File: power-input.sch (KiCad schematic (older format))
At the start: 13 parts, among them Q1 WST03P06

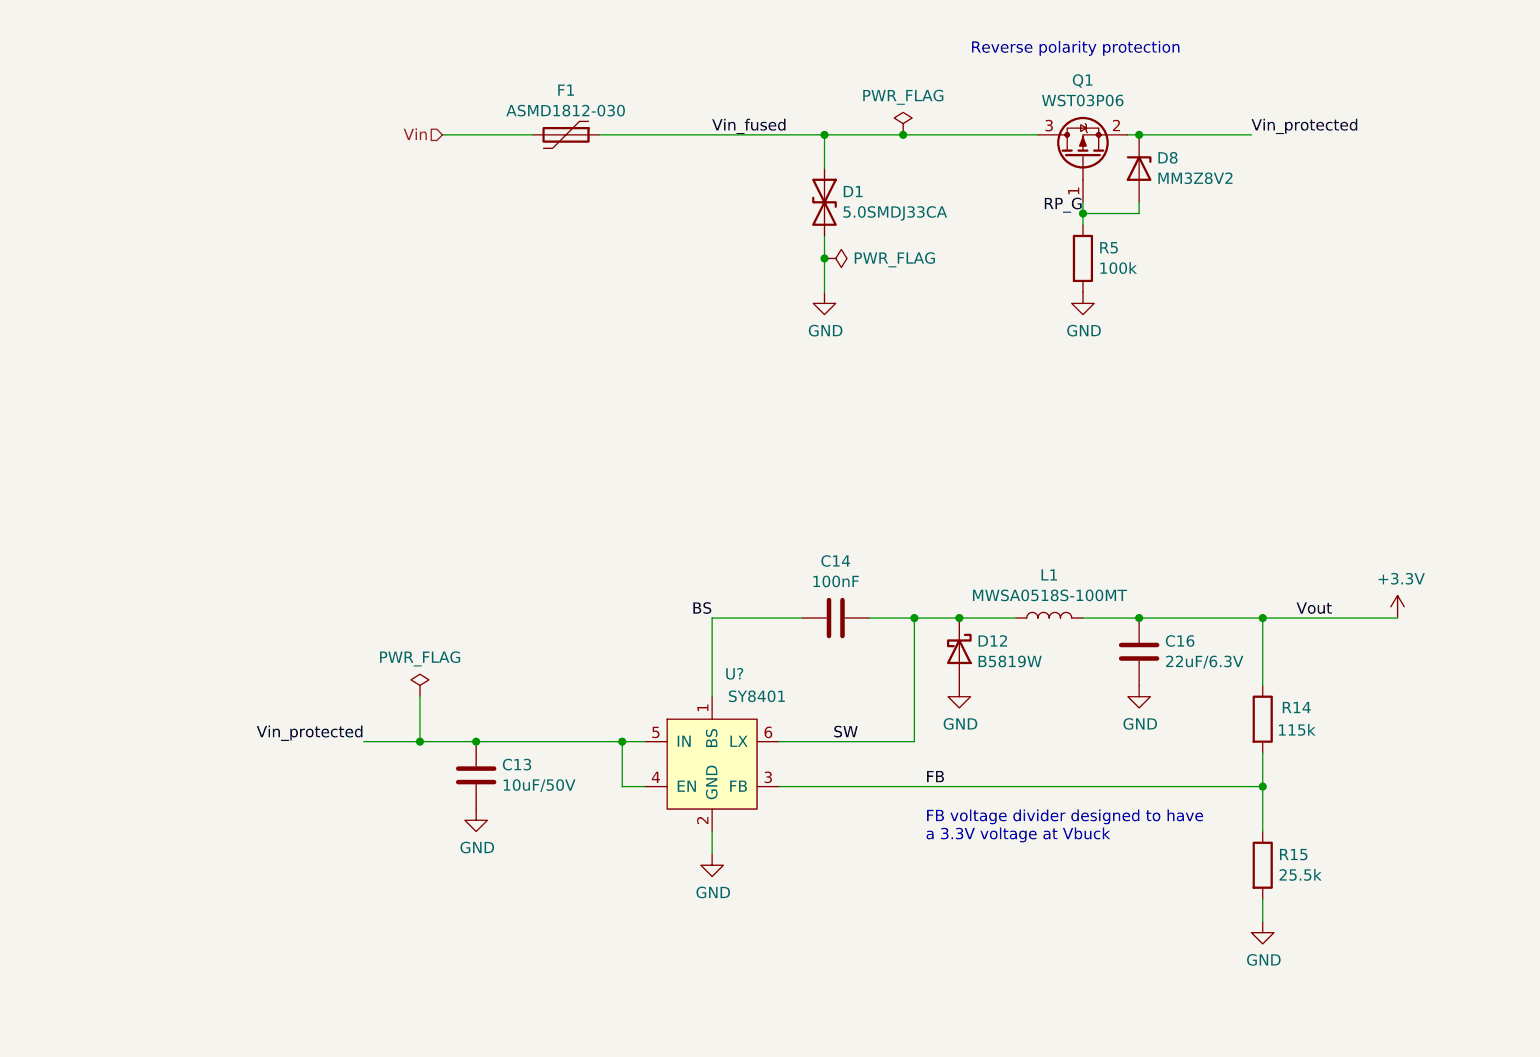
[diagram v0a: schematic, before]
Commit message: Update according to comments
Also add missing connectors and update the fuses
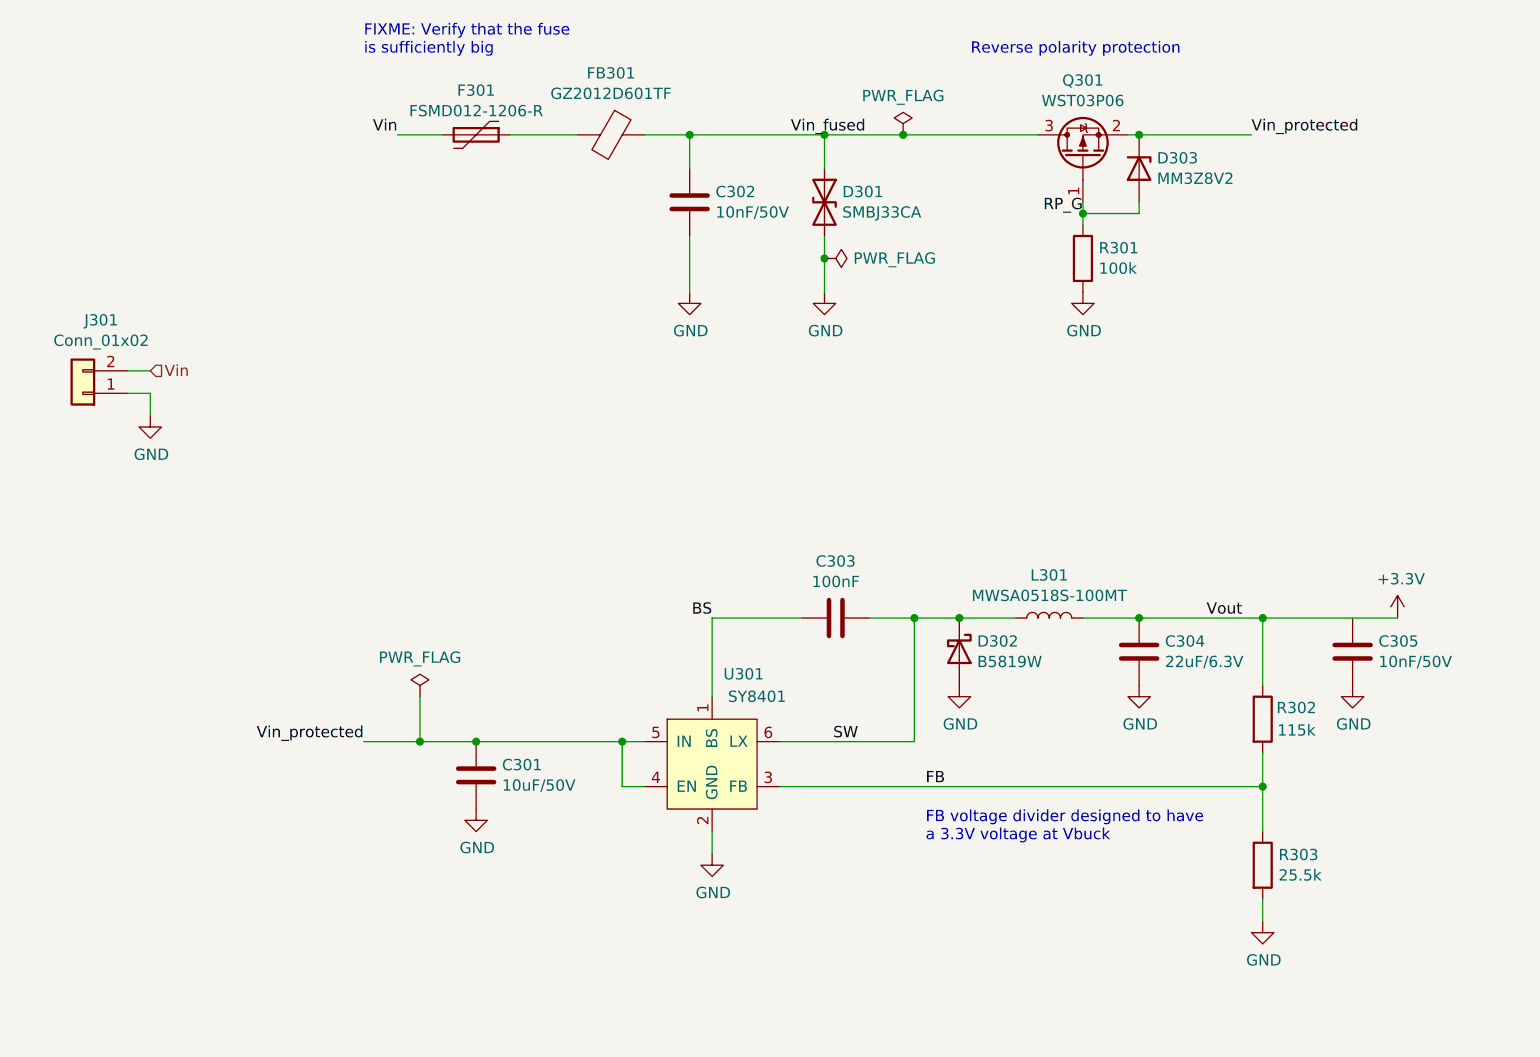
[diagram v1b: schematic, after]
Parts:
- removed D1: 5.0SMDJ33CA, Diode_SMD:D_SMC, symbol Device:D_TVS
- removed U?: SY8401, symbol SH-ESP32:SY8401
- added C302, C305: 10nF/50V, symbol Device:C
- added D301: SMBJ33CA, Diode_SMD:D_SMB, symbol Device:D_TVS
- added FB301: GZ2012D601TF, symbol Device:Ferrite_Bead
- added J301: Conn_01x02, symbol Connector_Generic:Conn_01x02
- added U301: SY8401, symbol SH-ESP32:SY8401
- F301: renamed from F1; value ASMD1812-030 -> FSMD012-1206-R
- renumbered C13 to C301, C14 to C303, C16 to C304, D12 to D302, D8 to D303, L1 to L301, Q1 to Q301, R5 to R301, R14 to R302, R15 to R303
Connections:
- net BS: now also U301.1 (BS)
- net FB: now also U301.3 (FB)
- net GND: now also C302.2, C305.2, D301.2 (A2), J301.1 (Pin_1), U301.2 (GND)
- net SW: now also U301.6 (LX)
- net Vin: now also J301.2 (Pin_2)
- net Vin_fused: now also C302.1, D301.1 (A1), FB301.1; no longer F301.1
- net Vin_protected: now also U301.4 (EN), U301.5 (IN)
- new net: F301.1, FB301.2
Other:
- note added: "FIXME: Verify that the fuse\nis sufficiently big"
- moved on the sheet: F301

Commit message: Rough PCB layout
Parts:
- C302, C305: footprint (none) -> Capacitor_SMD:C_0402_1005Metric
- D302: footprint (none) -> Diode_SMD:D_SOD-123
- F301: footprint (none) -> Fuse:Fuse_1206_3216Metric
- FB301: footprint (none) -> Inductor_SMD:L_0805_2012Metric
- J301: footprint (none) -> Connector_Phoenix_MC:PhoenixContact_MCV_1,5_2-G-3.81_1x02_P3.81mm_Vertical
- L301: footprint (none) -> Inductor_SMD:L_Sunlord_MWSA0518_5.4x5.2mm
- R301: footprint Resistor_SMD:R_0603_1608Metric -> Resistor_SMD:R_0402_1005Metric
- U301: footprint (none) -> Package_TO_SOT_SMD:SOT-23-6
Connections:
- net +3V3: now also C305.1
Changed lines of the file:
@@
 F 0 "F301" V 3653 2100 50  0000 C CNN
 F 1 "FSMD012-1206-R" V 3744 2100 50  0000 C CNN
-F 2 "" V 3780 2100 50  0001 C CNN
+F 2 "Fuse:Fuse_1206_3216Metric" V 3780 2100 50  0001 C CNN
 F 3 "~" H 3850 2100 50  0001 C CNN
 F 4 "" H 3850 2100 50  0001 C CNN "LCSC"
@@
 	1    0    0    -1
 $EndComp
-Wire Wire Line
-	5400 2550 5400 2650
-Connection ~ 5400 2650
-Wire Wire Line
-	5400 2650 5400 2800
 $Comp
 L Transistor_FET:Si2371EDS Q?
@@
 F 0 "R301" H 6620 2696 50  0000 L CNN
 F 1 "100k" H 6620 2605 50  0000 L CNN
-F 2 "Resistor_SMD:R_0603_1608Metric" V 6480 2650 50  0001 C CNN
+F 2 "Resistor_SMD:R_0402_1005Metric" V 6480 2650 50  0001 C CNN
 F 3 "~" H 6550 2650 50  0001 C CNN
 F 4 "C25803" H 6550 2650 50  0001 C CNN "LCSC"
@@
 Wire Wire Line
 	5750 2100 6350 2100
-$Comp
-L power:PWR_FLAG #FLG?
-U 1 1 5E475BD3
-P 5400 2650
-AR Path="/5E475BD3" Ref="#FLG?"  Part="1"
-AR Path="/5E460E30/5E475BD3" Ref="#FLG?"  Part="1"
-AR Path="/5F6FAF6E/5E475BD3" Ref="#FLG0302"  Part="1"
-F 0 "#FLG0302" H 5400 2725 50  0001 C CNN
-F 1 "PWR_FLAG" V 5400 2778 50  0000 L CNN
-F 2 "" H 5400 2650 50  0001 C CNN
-F 3 "~" H 5400 2650 50  0001 C CNN
-	1    5400 2650
-	0    1    -1   0
-$EndComp
 Text Label 6550 2450 2    50   ~ 0
 RP_G
@@
 F 0 "L301" V 6590 4250 50  0000 C CNN
 F 1 "MWSA0518S-100MT" V 6499 4250 50  0000 C CNN
-F 2 "" H 6400 4250 50  0001 C CNN
+F 2 "Inductor_SMD:L_Sunlord_MWSA0518_5.4x5.2mm" H 6400 4250 50  0001 C CNN
 F 3 "~" H 6400 4250 50  0001 C CNN
 F 4 "" V 6400 4250 50  0001 C CNN "URL"
@@
 F 0 "D302" V 5954 4479 50  0000 L CNN
 F 1 "B5819W" V 6045 4479 50  0000 L CNN
-F 2 "" H 6000 4400 50  0001 C CNN
+F 2 "Diode_SMD:D_SOD-123" H 6000 4400 50  0001 C CNN
 F 3 "~" H 6000 4400 50  0001 C CNN
 F 4 "" V 6000 4400 50  0001 C CNN "Notes"
@@
 F 0 "FB301" V 4176 2100 50  0000 C CNN
 F 1 "GZ2012D601TF" V 4267 2100 50  0000 C CNN
-F 2 "" V 4380 2100 50  0001 C CNN
+F 2 "Inductor_SMD:L_0805_2012Metric" V 4380 2100 50  0001 C CNN
 F 3 "~" H 4450 2100 50  0001 C CNN
 	1    4450 2100
@@
 F 0 "C302" H 4915 2446 50  0000 L CNN
 F 1 "10nF/50V" H 4915 2355 50  0000 L CNN
-F 2 "" H 4838 2250 50  0001 C CNN
+F 2 "Capacitor_SMD:C_0402_1005Metric" H 4838 2250 50  0001 C CNN
 F 3 "~" H 4800 2400 50  0001 C CNN
 	1    4800 2400
@@
 F 0 "U301" H 4950 5400 50  0000 L CNN
 F 1 "SY8401" H 5100 5300 50  0000 C CNN
-F 2 "" H 4750 4950 50  0001 C CNN
+F 2 "Package_TO_SOT_SMD:SOT-23-6" H 4750 4950 50  0001 C CNN
 F 3 "" H 4750 4950 50  0001 C CNN
 	1    4900 4950
@@
 	6800 4250 7350 4250
 Wire Wire Line
-	7350 4250 7950 4250
+	7350 4250 7750 4250
 Connection ~ 7350 4250
 Connection ~ 7350 5000
@@
 F 0 "C305" H 7865 4446 50  0000 L CNN
 F 1 "10nF/50V" H 7865 4355 50  0000 L CNN
-F 2 "" H 7788 4250 50  0001 C CNN
+F 2 "Capacitor_SMD:C_0402_1005Metric" H 7788 4250 50  0001 C CNN
 F 3 "~" H 7750 4400 50  0001 C CNN
 	1    7750 4400
@@
 F 0 "J301" H 2018 2925 50  0000 C CNN
 F 1 "Conn_01x02" H 2018 3016 50  0000 C CNN
-F 2 "" H 2100 3250 50  0001 C CNN
+F 2 "Connector_Phoenix_MC:PhoenixContact_MCV_1,5_2-G-3.81_1x02_P3.81mm_Vertical" H 2100 3250 50  0001 C CNN
 F 3 "~" H 2100 3250 50  0001 C CNN
 	1    2100 3250
@@
 Wire Wire Line
 	2400 3150 2300 3150
-Text HLabel 2400 3150 2    50   Input ~ 0
-Vin
 $Comp
 L Device:D_TVS D?
@@
 Text Notes 3350 1750 0    50   ~ 0
 FIXME: Verify that the fuse\nis sufficiently big
+Text Label 2400 3150 0    50   ~ 0
+Vin
+Wire Wire Line
+	5400 2550 5400 2800
+Connection ~ 7750 4250
+Wire Wire Line
+	7750 4250 7950 4250
 $EndSCHEMATC

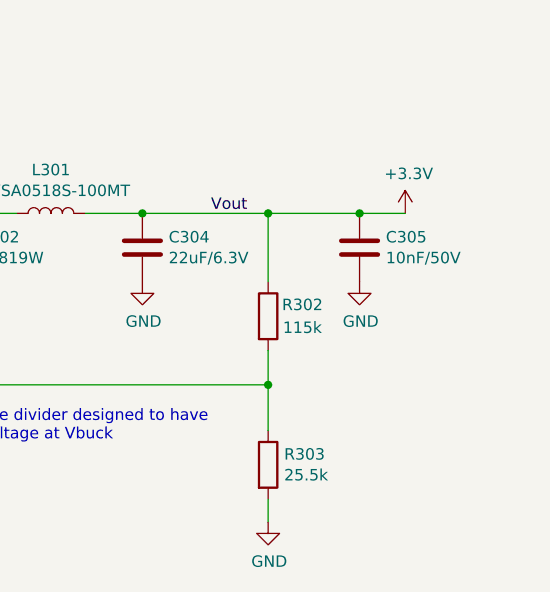
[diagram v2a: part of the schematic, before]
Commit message: Specified JLCPCB footprints for components
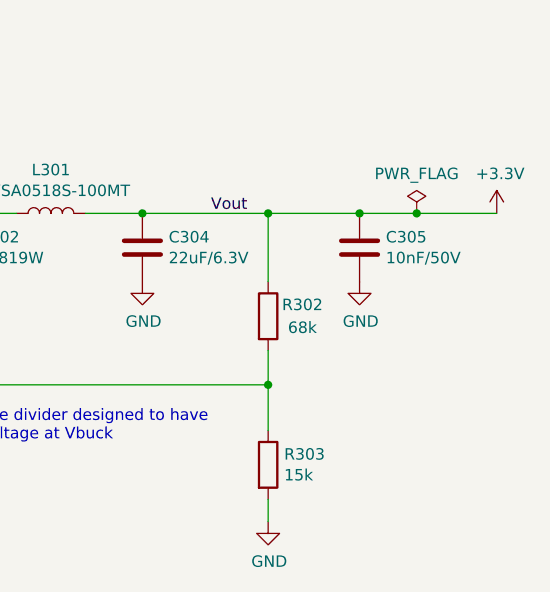
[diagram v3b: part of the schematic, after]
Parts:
- C302, C305: LCSC (none) -> C15195
- C303: footprint Capacitor_SMD:C_0603_1608Metric -> Capacitor_SMD:C_0402_1005Metric; LCSC C14663 -> C1525
- F301: LCSC (none) -> C220144
- FB301: LCSC (none) -> C1017
- J301: LCSC (none) -> C8396
- R301: LCSC C25803 -> C25741
- R302: value 115k -> 68k; LCSC C25747 -> C36871
- R303: value 25.5k -> 15k; LCSC C26970 -> C25756
- U301: LCSC (none) -> C125906
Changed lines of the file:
@@
 F 2 "Fuse:Fuse_1206_3216Metric" V 3780 2100 50  0001 C CNN
 F 3 "~" H 3850 2100 50  0001 C CNN
-F 4 "" H 3850 2100 50  0001 C CNN "LCSC"
+F 4 "C220144" H 3850 2100 50  0001 C CNN "LCSC"
 	1    3850 2100
 	0    1    1    0
@@
 F 2 "Resistor_SMD:R_0402_1005Metric" V 6480 2650 50  0001 C CNN
 F 3 "~" H 6550 2650 50  0001 C CNN
-F 4 "C25803" H 6550 2650 50  0001 C CNN "LCSC"
+F 4 "C25741" H 6550 2650 50  0001 C CNN "LCSC"
 	1    6550 2650
 	1    0    0    -1
@@
 F 0 "C303" V 5198 4250 50  0000 C CNN
 F 1 "100nF" V 5289 4250 50  0000 C CNN
-F 2 "Capacitor_SMD:C_0603_1608Metric" H 5488 4100 50  0001 C CNN
+F 2 "Capacitor_SMD:C_0402_1005Metric" H 5488 4100 50  0001 C CNN
 F 3 "~" H 5450 4250 50  0001 C CNN
-F 4 "C14663" H 5450 4250 50  0001 C CNN "LCSC"
+F 4 "C1525" H 5450 4250 50  0001 C CNN "LCSC"
 	1    5450 4250
 	0    1    1    0
@@
 L power:+3.3V #PWR0310
 U 1 1 5F80ACBB
-P 7950 4250
-F 0 "#PWR0310" H 7950 4100 50  0001 C CNN
-F 1 "+3.3V" H 7965 4423 50  0000 C CNN
-F 2 "" H 7950 4250 50  0001 C CNN
-F 3 "" H 7950 4250 50  0001 C CNN
-	1    7950 4250
+P 8350 4250
+F 0 "#PWR0310" H 8350 4100 50  0001 C CNN
+F 1 "+3.3V" H 8365 4423 50  0000 C CNN
+F 2 "" H 8350 4250 50  0001 C CNN
+F 3 "" H 8350 4250 50  0001 C CNN
+	1    8350 4250
 	1    0    0    -1
 $EndComp
@@
 F 2 "Inductor_SMD:L_0805_2012Metric" V 4380 2100 50  0001 C CNN
 F 3 "~" H 4450 2100 50  0001 C CNN
+F 4 "C1017" H 4450 2100 50  0001 C CNN "LCSC"
 	1    4450 2100
 	0    1    1    0
@@
 F 2 "Capacitor_SMD:C_0402_1005Metric" H 4838 2250 50  0001 C CNN
 F 3 "~" H 4800 2400 50  0001 C CNN
+F 4 "C15195" H 4800 2400 50  0001 C CNN "LCSC"
 	1    4800 2400
 	1    0    0    -1
@@
 F 2 "Package_TO_SOT_SMD:SOT-23-6" H 4750 4950 50  0001 C CNN
 F 3 "" H 4750 4950 50  0001 C CNN
+F 4 "C125906" H 4900 4950 50  0001 C CNN "LCSC"
 	1    4900 4950
 	1    0    0    -1
@@
 AR Path="/5F6FAF6E/5CA62D90" Ref="R302"  Part="1"
 F 0 "R302" H 7500 4750 50  0000 C CNN
-F 1 "115k" H 7500 4650 50  0000 C CNN
+F 1 "68k" H 7500 4650 50  0000 C CNN
 F 2 "Resistor_SMD:R_0402_1005Metric" V 7280 4700 50  0001 C CNN
 F 3 "~" H 7350 4700 50  0001 C CNN
-F 4 "C25747" H 7350 4700 50  0001 C CNN "LCSC"
+F 4 "C36871" H 7350 4700 50  0001 C CNN "LCSC"
 	1    7350 4700
 	1    0    0    -1
@@
 AR Path="/5F6FAF6E/5CA62D89" Ref="R303"  Part="1"
 F 0 "R303" H 7420 5396 50  0000 L CNN
-F 1 "25.5k" H 7420 5305 50  0000 L CNN
+F 1 "15k" H 7420 5305 50  0000 L CNN
 F 2 "Resistor_SMD:R_0402_1005Metric" V 7280 5350 50  0001 C CNN
 F 3 "~" H 7350 5350 50  0001 C CNN
-F 4 "C26970" H 7350 5350 50  0001 C CNN "LCSC"
+F 4 "C25756" H 7350 5350 50  0001 C CNN "LCSC"
 	1    7350 5350
 	1    0    0    -1
@@
 F 2 "Capacitor_SMD:C_0402_1005Metric" H 7788 4250 50  0001 C CNN
 F 3 "~" H 7750 4400 50  0001 C CNN
+F 4 "C15195" H 7750 4400 50  0001 C CNN "LCSC"
 	1    7750 4400
 	1    0    0    -1
@@
 F 2 "Connector_Phoenix_MC:PhoenixContact_MCV_1,5_2-G-3.81_1x02_P3.81mm_Vertical" H 2100 3250 50  0001 C CNN
 F 3 "~" H 2100 3250 50  0001 C CNN
+F 4 "C8396" H 2100 3250 50  0001 C CNN "LCSC"
 	1    2100 3250
 	-1   0    0    1
@@
 Connection ~ 7750 4250
 Wire Wire Line
-	7750 4250 7950 4250
+	7750 4250 8000 4250
+$Comp
+L power:PWR_FLAG #FLG0101
+U 1 1 5FAE11E1
+P 8000 4250
+F 0 "#FLG0101" H 8000 4325 50  0001 C CNN
+F 1 "PWR_FLAG" H 8000 4423 50  0000 C CNN
+F 2 "" H 8000 4250 50  0001 C CNN
+F 3 "~" H 8000 4250 50  0001 C CNN
+	1    8000 4250
+	1    0    0    -1
+$EndComp
+Connection ~ 8000 4250
+Wire Wire Line
+	8000 4250 8350 4250
 $EndSCHEMATC

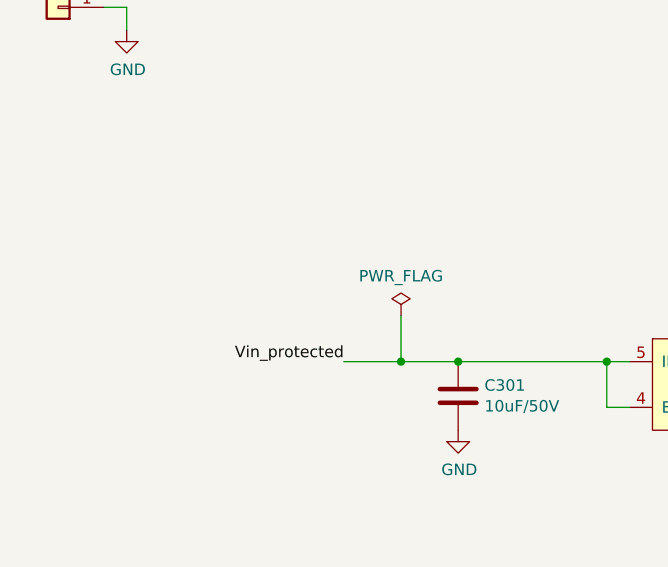
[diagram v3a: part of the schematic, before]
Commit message: Trace USB 5V to buck converter input
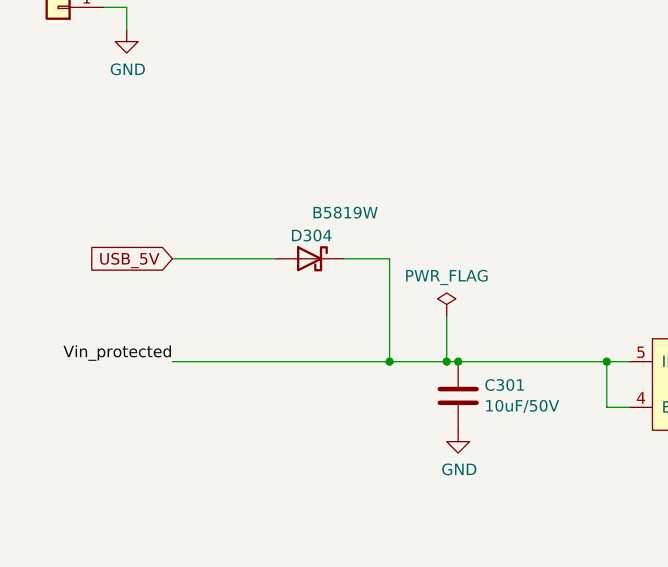
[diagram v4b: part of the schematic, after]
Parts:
- added D304: B5819W, Diode_SMD:D_SOD-123, symbol Device:D_Schottky
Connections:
- net Vin_protected: now also D304.1 (K)
- new net USB_5V: D304.2 (A)
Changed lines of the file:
@@
 L power:PWR_FLAG #FLG?
 U 1 1 5CA62DDA
-P 3600 4600
+P 3800 4600
 AR Path="/5C3476D8/5CA62DDA" Ref="#FLG?"  Part="1"
 AR Path="/5CA65CC5/5CA62DDA" Ref="#FLG?"  Part="1"
 AR Path="/5F6FAF6E/5CA62DDA" Ref="#FLG0301"  Part="1"
-F 0 "#FLG0301" H 3600 4675 50  0001 C CNN
-F 1 "PWR_FLAG" H 3600 4774 50  0000 C CNN
-F 2 "" H 3600 4600 50  0001 C CNN
-F 3 "~" H 3600 4600 50  0001 C CNN
-	1    3600 4600
-	1    0    0    -1
-$EndComp
-Wire Wire Line
-	3600 4600 3600 4800
-Connection ~ 3600 4800
+F 0 "#FLG0301" H 3800 4675 50  0001 C CNN
+F 1 "PWR_FLAG" H 3800 4774 50  0000 C CNN
+F 2 "" H 3800 4600 50  0001 C CNN
+F 3 "~" H 3800 4600 50  0001 C CNN
+	1    3800 4600
+	1    0    0    -1
+$EndComp
+Wire Wire Line
+	3800 4600 3800 4800
 Text Label 5550 4800 2    50   ~ 0
 SW
@@
 Wire Wire Line
 	5800 4250 5800 4800
-Wire Wire Line
-	3600 4800 3850 4800
 Connection ~ 3850 4800
 Wire Wire Line
 	3850 4800 4500 4800
-Wire Wire Line
-	3350 4800 3600 4800
 Wire Wire Line
 	4600 5000 4500 5000
@@
 Text Label 7300 2100 0    50   ~ 0
 Vin_protected
-Text Label 3350 4800 2    50   ~ 0
+Text Label 2600 4800 2    50   ~ 0
 Vin_protected
 Connection ~ 6800 4250
@@
 Wire Wire Line
 	8000 4250 8350 4250
+$Comp
+L Device:D_Schottky D?
+U 1 1 5FAEC660
+P 3200 4350
+AR Path="/5C3476D8/5FAEC660" Ref="D?"  Part="1"
+AR Path="/5CA65CC5/5FAEC660" Ref="D?"  Part="1"
+AR Path="/5F6FAF6E/5FAEC660" Ref="D304"  Part="1"
+F 0 "D304" H 3100 4450 50  0000 L CNN
+F 1 "B5819W" H 2900 4550 50  0000 L CNN
+F 2 "Diode_SMD:D_SOD-123" H 3200 4350 50  0001 C CNN
+F 3 "~" H 3200 4350 50  0001 C CNN
+F 4 "" V 3200 4350 50  0001 C CNN "Notes"
+F 5 "C8598" H 3200 4350 50  0001 C CNN "LCSC"
+	1    3200 4350
+	-1   0    0    -1
+$EndComp
+Connection ~ 3800 4800
+Wire Wire Line
+	3800 4800 3850 4800
+Wire Wire Line
+	2600 4800 3550 4800
+Wire Wire Line
+	3350 4350 3550 4350
+Wire Wire Line
+	3550 4350 3550 4800
+Connection ~ 3550 4800
+Wire Wire Line
+	3550 4800 3800 4800
+Wire Wire Line
+	3050 4350 2600 4350
+Text GLabel 2600 4350 0    50   Input ~ 0
+USB_5V
 $EndSCHEMATC
